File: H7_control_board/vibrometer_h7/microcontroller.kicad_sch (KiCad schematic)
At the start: 30 parts, among them J201 Conn_01x04_Socket, J202 Conn_ST_STDC14, J203 TC2030-NL, Q201 BSS138, Q202 BSS138, SW201 SW_Push, U201 STM32H723VGTx, Y201 24MHz

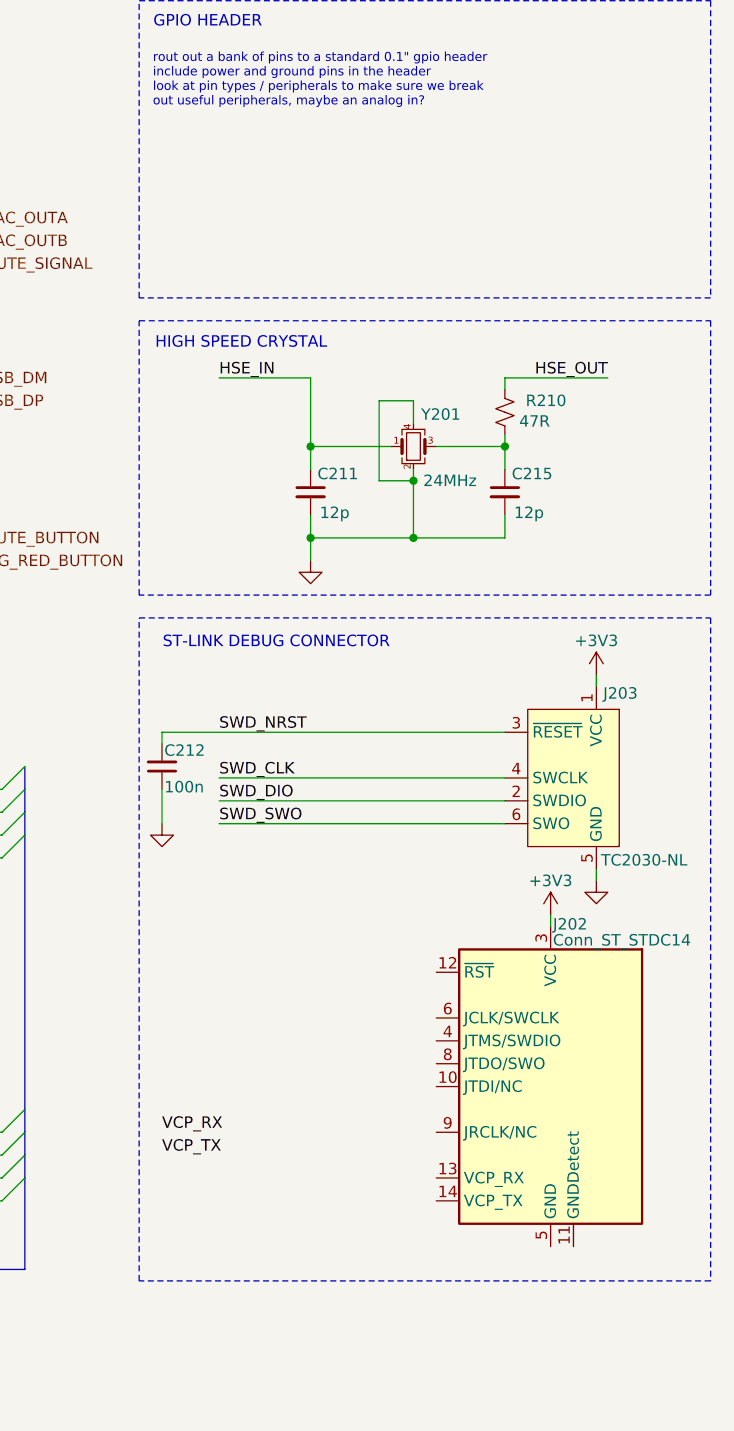
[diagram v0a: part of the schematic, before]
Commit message: worked on power supply filtering
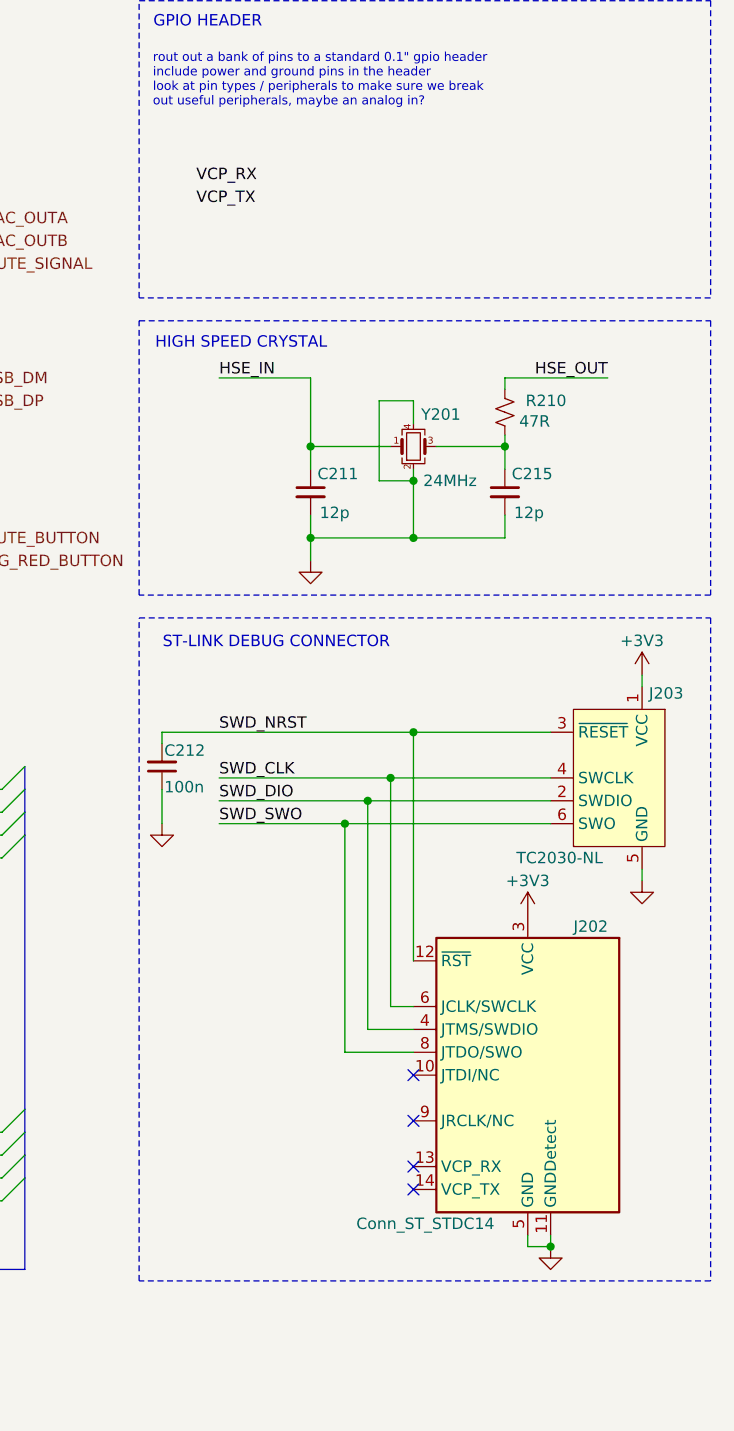
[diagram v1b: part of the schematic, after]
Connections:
- net GND: now also J202.11 (GNDDetect), J202.5 (GND), J202.7 (GND)
- net SWD_CLK: now also J202.6 (JCLK/SWCLK)
- net SWD_DIO: now also J202.4 (JTMS/SWDIO)
- net SWD_NRST: now also J202.12 (~{RST})
- net SWD_SWO: now also J202.8 (JTDO/SWO)
- no-connect marks 46 -> 50
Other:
- moved on the sheet: J202, J203

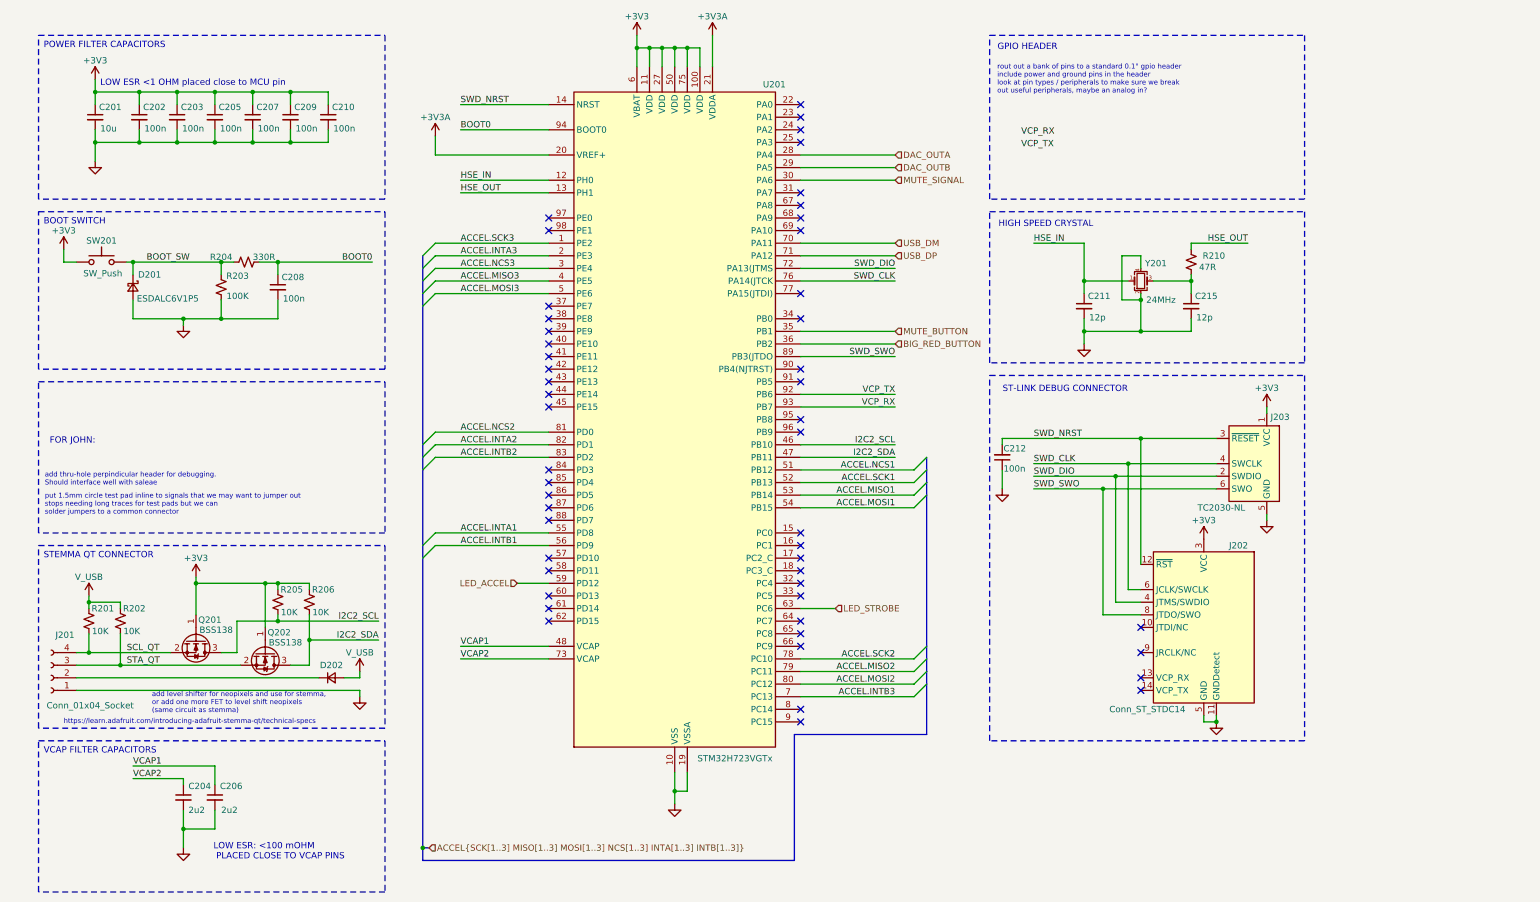
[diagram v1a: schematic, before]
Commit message: more decoupling caps, added level shifter to ws2812 led signal line
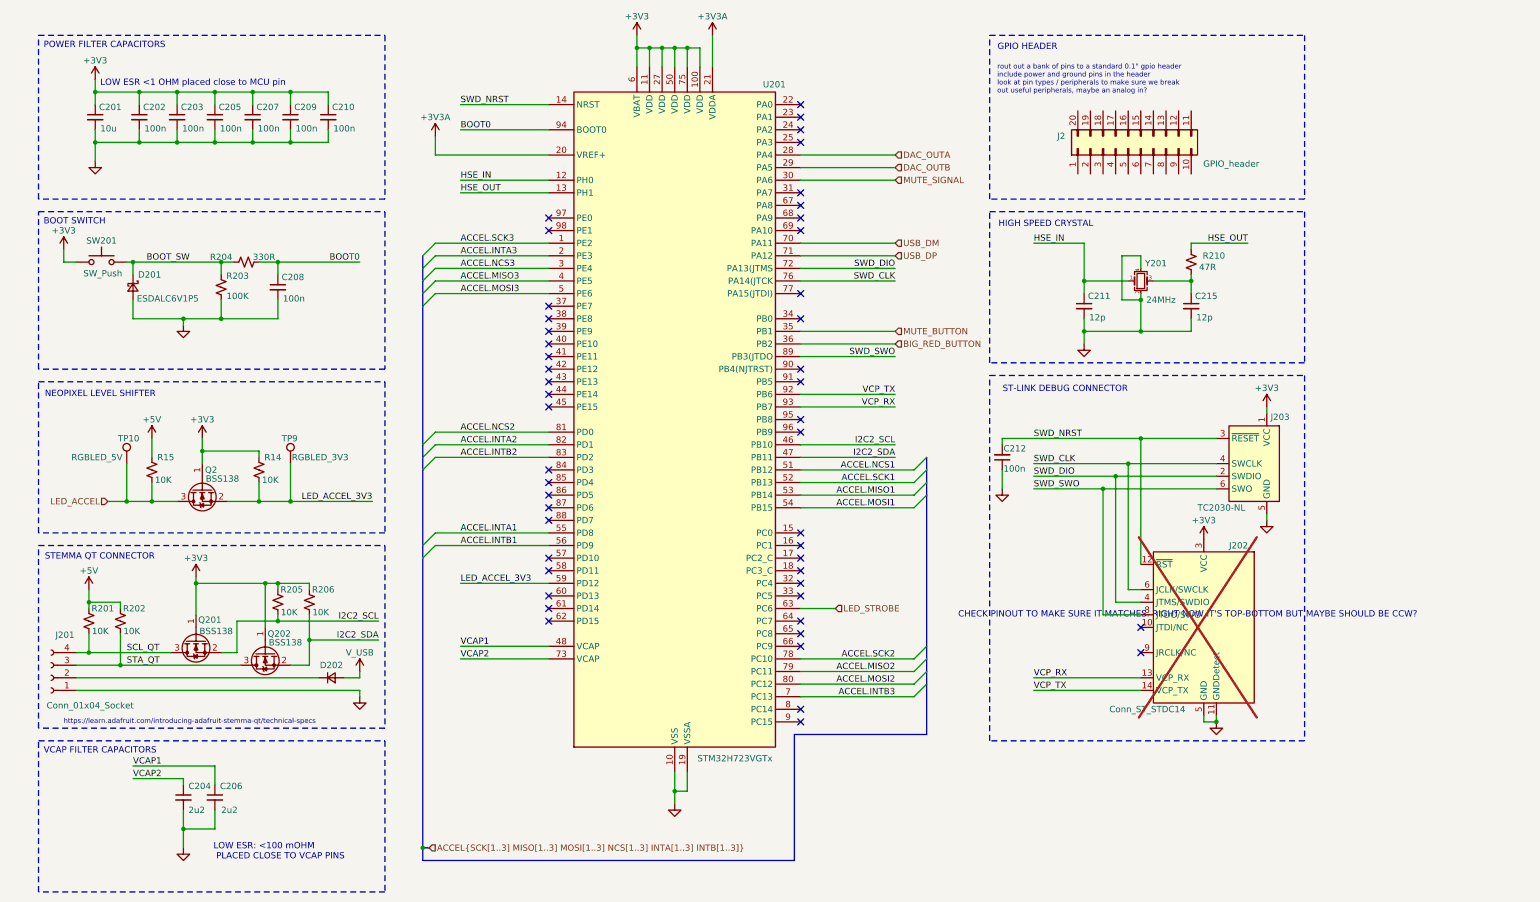
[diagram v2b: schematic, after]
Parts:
- added J2: GPIO_header, symbol Connector_Generic:Conn_02x10_Counter_Clockwise
- added Q2: BSS138, Package_TO_SOT_SMD:SOT-23, symbol Transistor_FET:BSS138
- added R14, R15: 10K, symbol Device:R_Small_US
- added TP10: RGBLED_5V, symbol Connector:TestPoint
- added TP9: RGBLED_3V3, symbol Connector:TestPoint
- J202: footprint (none) -> Connector_PinHeader_1.27mm:PinHeader_2x07_P1.27mm_Vertical_SMD; now not fitted
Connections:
- net +3V3: now also Q2.1 (G), R14.2
- net I2C2_SCL: now also Q201.2 (S); no longer Q201.3 (D)
- net I2C2_SDA: now also Q202.2 (S); no longer Q202.3 (D)
- net LED_ACCEL: now also Q2.3 (D), R15.1, TP10.1; no longer U201.59 (PD12)
- net SCL_QT: now also Q201.3 (D); no longer Q201.2 (S)
- net STA_QT: now also Q202.3 (D); no longer Q202.2 (S)
- net VCP_RX: now also J202.13 (VCP_RX)
- net VCP_TX: now also J202.14 (VCP_TX)
- net V_USB: no longer R201.2, R202.2
- new net +5V: R15.2, R201.2, R202.2
- new net LED_ACCEL_3V3: Q2.2 (S), R14.1, TP9.1, U201.59 (PD12)
- no-connect marks 50 -> 48
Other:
- note added: "CHECK PINOUT TO MAKE SURE IT MATCHES. RIGHT NOW IT'S TOP-BOTTOM BUT MAYBE SHOULD BE CCW?"
- note added: "NEOPIXEL LEVEL SHIFTER"
- note added: "STEMMA QT CONNECTOR"
- note removed: "FOR JOHN:"
- note removed: "add level shifter for neopixels and use for stemma, or add one more FET to level shift neopixels (same circuit as stemma)"
- note removed: "add thru-hole perpindicular header for debugging. Should interface well with saleae"
- note removed: "put 1.5mm circle test pad inline to signals that we may want to jumper out stops needing long traces for test pads but we can solder jumpers to a common connector"
- moved on the sheet: Q201, Q202

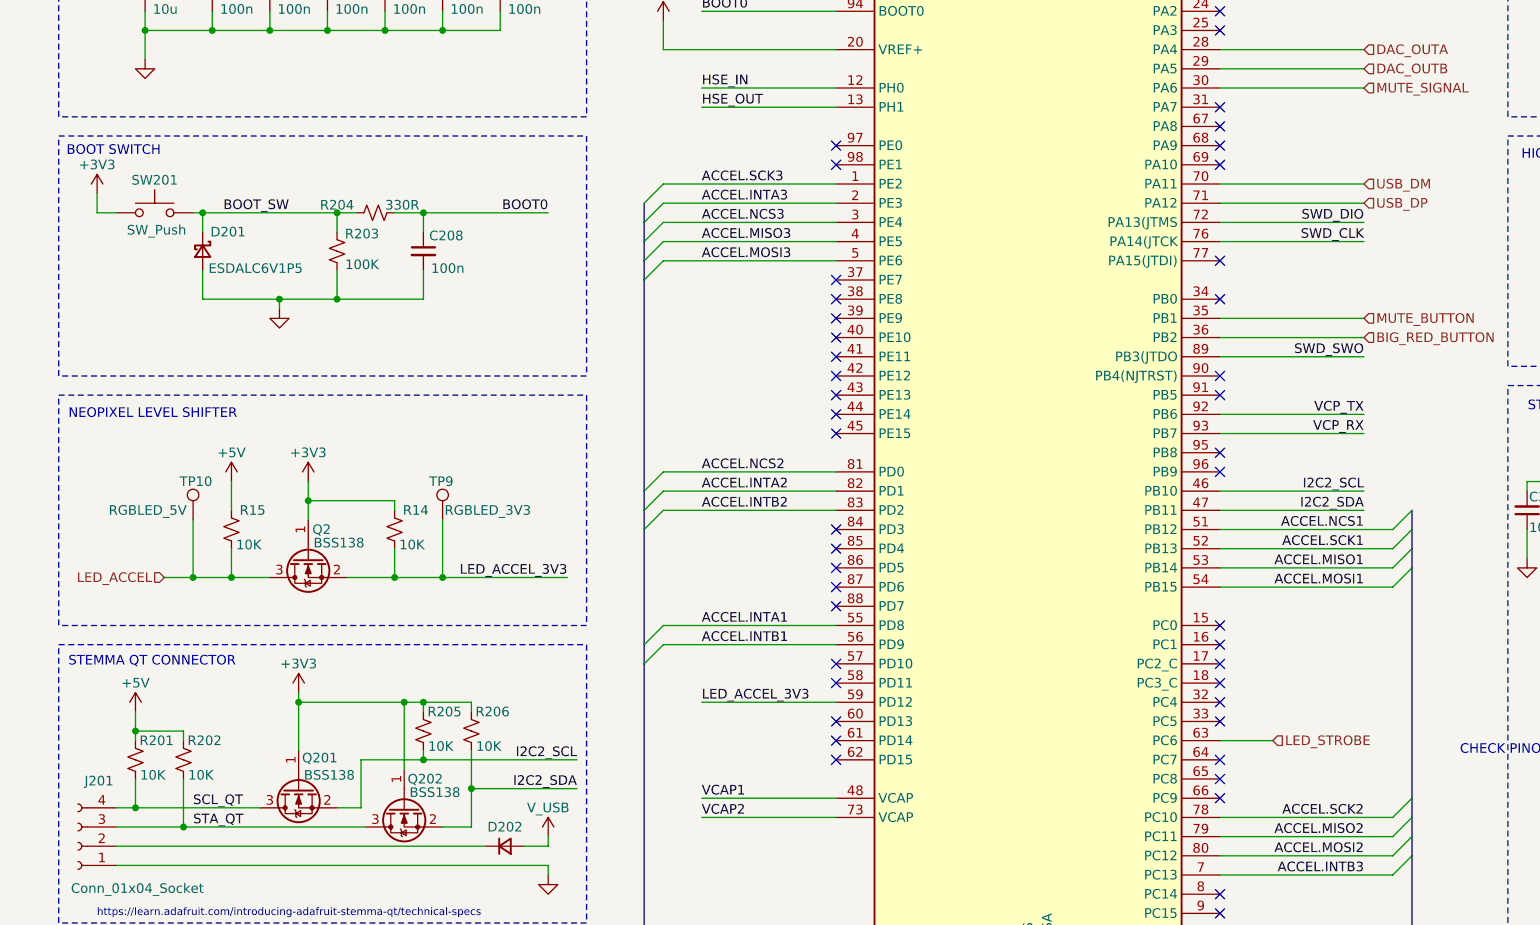
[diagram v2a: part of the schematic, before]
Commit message: selected strobe LEDs, schematic cleanup
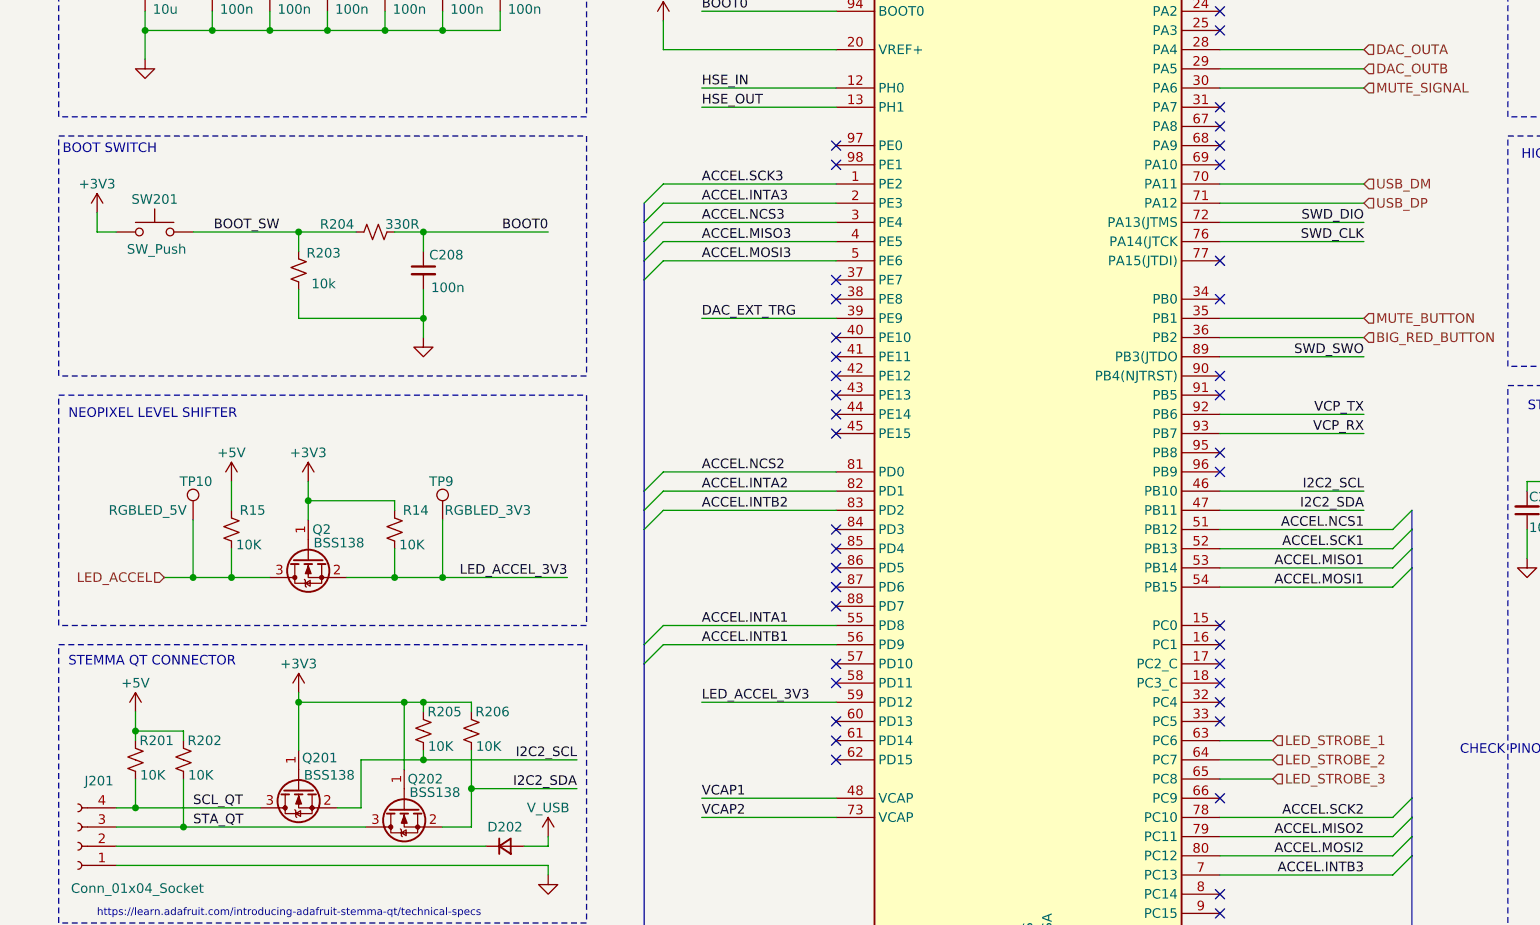
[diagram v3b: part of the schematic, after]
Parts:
- removed D201: ESDALC6V1P5, symbol Device:D_Schottky_Small
- R203: value 100K -> 10k
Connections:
- net DAC_EXT_TRG: now reaches U201.39 (PE9)
- net LED_STROBE_2: now reaches U201.64 (PC7)
- net LED_STROBE_3: now reaches U201.65 (PC8)
- net LED_STROBE renamed LED_STROBE_1
- no-connect marks 48 -> 45
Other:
- note added: "BOOT SWITCH"
- moved on the sheet: C208, R203, R204, SW201
